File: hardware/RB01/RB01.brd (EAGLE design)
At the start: 50 x 31 mm, 11 parts, among them J1 CON_TERMINAL_BLOCK_03-5MM, J2 CON_TERMINAL_BLOCK_02-5MM, K1 JS-M1-12V-5, Q1 BC337

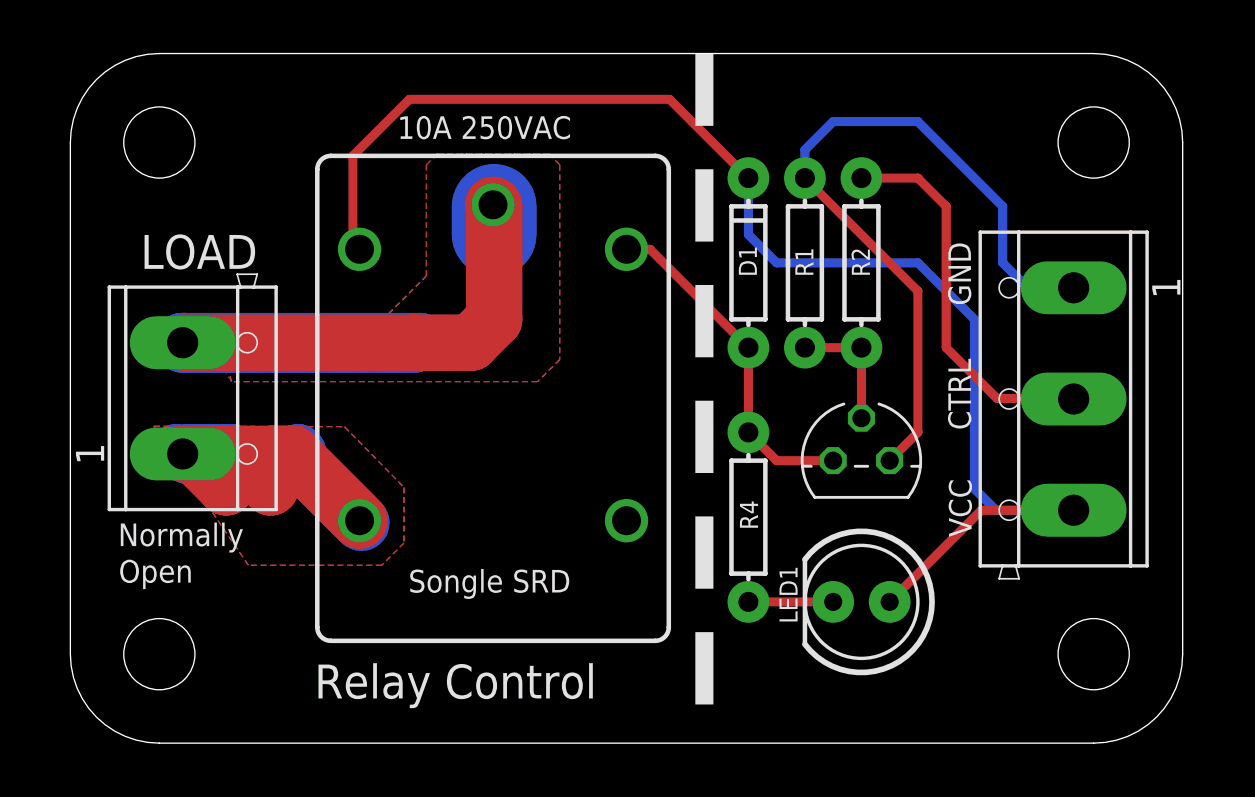
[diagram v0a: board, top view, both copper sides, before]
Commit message: hot traces on bottom only
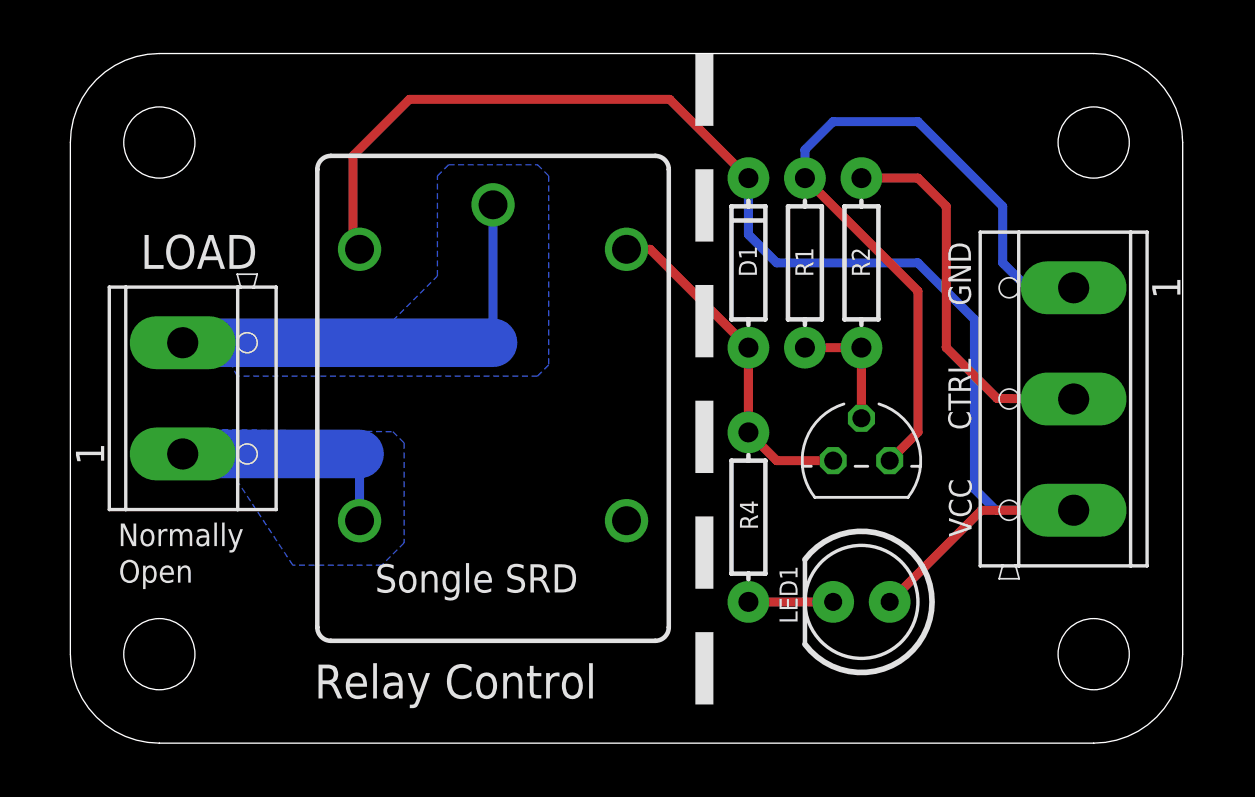
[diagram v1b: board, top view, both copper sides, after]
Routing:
- net LOAD2: track 74.1 -> 20.1 mm
- net LOAD1: track 53.2 -> 10.4 mm
- removed copper zone on layer 1, net LOAD1
- removed copper zone on layer 1, net LOAD2
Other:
- board text removed: "10A 250VAC"
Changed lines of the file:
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@@
 <board>
 <plain>
-<text x="14.692" y="27.162" size="1.016" layer="21" font="vector" ratio="15">10A 250VAC</text>
 <text x="40.483" y="19.661" size="1.016" layer="21" ratio="15" rot="R90">GND</text>
 <text x="40.513" y="9.271" size="1.016" layer="21" ratio="15" rot="R90">VCC</text>
@@
 <text x="2.143" y="8.858" size="1.016" layer="21" ratio="15">Normally</text>
 <text x="40.483" y="14.073" size="1.016" layer="21" ratio="15" rot="R90">CTRL</text>
-<text x="15.192" y="6.772" size="1.016" layer="21" font="vector" ratio="15">Songle SRD</text>
+<text x="13.692" y="6.772" size="1.27" layer="21" font="vector" ratio="15">Songle SRD</text>
 <rectangle x1="16.0163" y1="15.4879" x2="21.5789" y2="15.5133" layer="22" rot="R270"/>
 <rectangle x1="16.0163" y1="15.4879" x2="21.6297" y2="15.5133" layer="22" rot="R270"/>
@@
 <contactref element="K1" pad="C"/>
 <contactref element="J2" pad="2"/>
-<polygon width="0.254" layer="1">
+<polygon width="0.254" layer="16">
 <vertex x="6.746" y="17.97"/>
 <vertex x="8" y="19" curve="-60"/>
 <vertex x="8.1" y="19"/>
-<vertex x="14" y="19"/>
-<vertex x="16" y="21"/>
-<vertex x="16" y="26"/>
-<vertex x="16.5" y="26.5"/>
-<vertex x="21.5" y="26.5"/>
-<vertex x="22" y="26"/>
-<vertex x="22" y="17.25"/>
-<vertex x="21" y="16.25"/>
-<vertex x="7.25" y="16.25"/>
+<vertex x="14.5" y="19"/>
+<vertex x="16.5" y="21"/>
+<vertex x="16.5" y="25.5"/>
+<vertex x="17" y="26"/>
+<vertex x="21" y="26"/>
+<vertex x="21.5" y="25.5"/>
+<vertex x="21.5" y="17"/>
+<vertex x="21" y="16.5"/>
+<vertex x="7.5" y="16.5"/>
 </polygon>
-<polygon width="0.254" layer="16">
-<vertex x="6.246" y="17.97"/>
-<vertex x="8" y="19" curve="-60"/>
-<vertex x="8.1" y="19"/>
-<vertex x="14" y="19"/>
-<vertex x="16" y="21"/>
-<vertex x="16" y="26"/>
-<vertex x="16.5" y="26.5"/>
-<vertex x="21.5" y="26.5"/>
-<vertex x="22" y="26"/>
-<vertex x="22" y="17.25"/>
-<vertex x="21" y="16.25"/>
-<vertex x="7.25" y="16.25"/>
-</polygon>
-<wire x1="5.08" y1="18.034" x2="15.216" y2="18.034" width="2.1844" layer="16"/>
-<wire x1="15.216" y1="18.034" x2="15.5" y2="17.75" width="2.1844" layer="16"/>
-<wire x1="15.5" y1="17.75" x2="5" y2="17.75" width="2.1844" layer="16"/>
-<wire x1="5" y1="17.75" x2="15.25" y2="17.75" width="2.1844" layer="16"/>
-<wire x1="15.25" y1="17.75" x2="15.75" y2="18.25" width="2.1844" layer="16"/>
-<wire x1="15.75" y1="18.25" x2="5" y2="18.25" width="2.1844" layer="16"/>
-<wire x1="5" y1="18.25" x2="15.494" y2="18.034" width="2.1844" layer="16"/>
-<wire x1="5.05" y1="18" x2="15.46" y2="18" width="2.54" layer="1"/>
-<wire x1="15.46" y1="18" x2="18" y2="18" width="2.54" layer="1"/>
-<wire x1="18" y1="18" x2="19.05" y2="19.05" width="2.54" layer="1"/>
-<wire x1="19.05" y1="19.05" x2="19.05" y2="21.59" width="2.54" layer="1"/>
-<wire x1="19.05" y1="21.59" x2="19.05" y2="24.15" width="2.54" layer="1"/>
-<wire x1="19.05" y1="24.15" x2="19" y2="24.2" width="2.54" layer="1"/>
-<wire x1="19.05" y1="24.13" x2="19.05" y2="22.86" width="3.81" layer="16"/>
+<wire x1="5.05" y1="18" x2="19" y2="18" width="2.1844" layer="16"/>
+<wire x1="19" y1="18" x2="19" y2="24.2" width="0.4064" layer="16"/>
 </signal>
 <signal name="LOAD1">
 <contactref element="K1" pad="NO"/>
 <contactref element="J2" pad="1"/>
-<polygon width="0.254" layer="1">
-<vertex x="12.319" y="14.224"/>
-<vertex x="12.327" y="14.216"/>
-<vertex x="15" y="11.5"/>
+<polygon width="0.254" layer="16">
+<vertex x="14.5" y="14"/>
+<vertex x="15" y="13.5"/>
 <vertex x="15" y="9"/>
 <vertex x="14" y="8"/>
-<vertex x="8" y="8"/>
-<vertex x="3.75" y="14.25"/>
+<vertex x="10" y="8"/>
+<vertex x="5.9732375" y="14.101134375"/>
 </polygon>
-<wire x1="5.05" y1="13" x2="7" y2="13" width="2.54" layer="1"/>
-<wire x1="7" y1="13" x2="5.5" y2="13" width="2.54" layer="1"/>
-<wire x1="5.5" y1="13" x2="7" y2="11.5" width="2.54" layer="1"/>
-<wire x1="7" y1="11.5" x2="6" y2="13" width="2.54" layer="1"/>
-<wire x1="6" y1="13" x2="10" y2="13" width="2.54" layer="1"/>
-<wire x1="10" y1="13" x2="9" y2="12" width="2.54" layer="1"/>
-<wire x1="9" y1="12" x2="9" y2="11.5" width="2.54" layer="1"/>
-<wire x1="9" y1="11.5" x2="9" y2="13" width="2.54" layer="1"/>
-<wire x1="9" y1="13" x2="10" y2="13" width="2.54" layer="1"/>
-<wire x1="10" y1="13" x2="13" y2="10" width="2.54" layer="1"/>
-<polygon width="0.254" layer="16">
-<vertex x="12.319" y="14.224"/>
-<vertex x="12.327" y="14.216"/>
-<vertex x="15" y="11.5"/>
-<vertex x="15" y="9"/>
-<vertex x="14" y="8"/>
-<vertex x="8" y="8"/>
-<vertex x="3.75" y="14.25"/>
-</polygon>
-<wire x1="5.08" y1="13.081" x2="4.75" y2="13.25" width="2.1844" layer="16"/>
-<wire x1="4.75" y1="13.25" x2="5.25" y2="12.75" width="2.1844" layer="16"/>
-<wire x1="5.25" y1="12.75" x2="6.5" y2="12.75" width="2.1844" layer="16"/>
-<wire x1="6.5" y1="12.75" x2="6.5" y2="12.5" width="2.1844" layer="16"/>
-<wire x1="6.5" y1="12.5" x2="7.5" y2="12.75" width="2.1844" layer="16"/>
-<wire x1="7.5" y1="12.75" x2="7.25" y2="13" width="2.1844" layer="16"/>
-<wire x1="7.25" y1="13" x2="5" y2="13" width="2.1844" layer="16"/>
-<wire x1="5" y1="13" x2="5.25" y2="13.25" width="2.1844" layer="16"/>
-<wire x1="5.25" y1="13.25" x2="7.5" y2="13" width="2.1844" layer="16"/>
-<wire x1="7.5" y1="13" x2="7.25" y2="13.25" width="2.1844" layer="16"/>
-<wire x1="7.25" y1="13.25" x2="5.5" y2="13.25" width="2.1844" layer="16"/>
-<wire x1="5.5" y1="13.25" x2="5.5" y2="13" width="2.1844" layer="16"/>
-<wire x1="5.5" y1="13" x2="6.5" y2="13" width="2.1844" layer="16"/>
-<wire x1="6.5" y1="13" x2="6.5" y2="12.75" width="2.1844" layer="16"/>
-<wire x1="6.5" y1="12.5" x2="6" y2="12.5" width="2.1844" layer="16"/>
-<wire x1="6" y1="12.5" x2="10.25" y2="13.25" width="2.1844" layer="16"/>
-<wire x1="10.25" y1="13.25" x2="10.406" y2="13.094" width="2.1844" layer="16"/>
-<wire x1="10.406" y1="13.094" x2="7" y2="11.5" width="2.1844" layer="16"/>
-<wire x1="7" y1="11.5" x2="5.406" y2="13.094" width="2.1844" layer="16"/>
-<wire x1="5.406" y1="13.094" x2="5" y2="13.094" width="2.1844" layer="16"/>
-<wire x1="5" y1="13.094" x2="5" y2="13" width="2.1844" layer="16"/>
-<wire x1="5" y1="13" x2="10.406" y2="12.581" width="2.1844" layer="16"/>
-<wire x1="10.406" y1="12.581" x2="13.081" y2="9.906" width="2.54" layer="16"/>
+<wire x1="5.05" y1="13" x2="13" y2="13" width="2.1844" layer="16"/>
+<wire x1="13" y1="13" x2="13" y2="10.5" width="0.4064" layer="16"/>
 </signal>
 <signal name="VCC">

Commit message: faster higher-power diode closer to coil
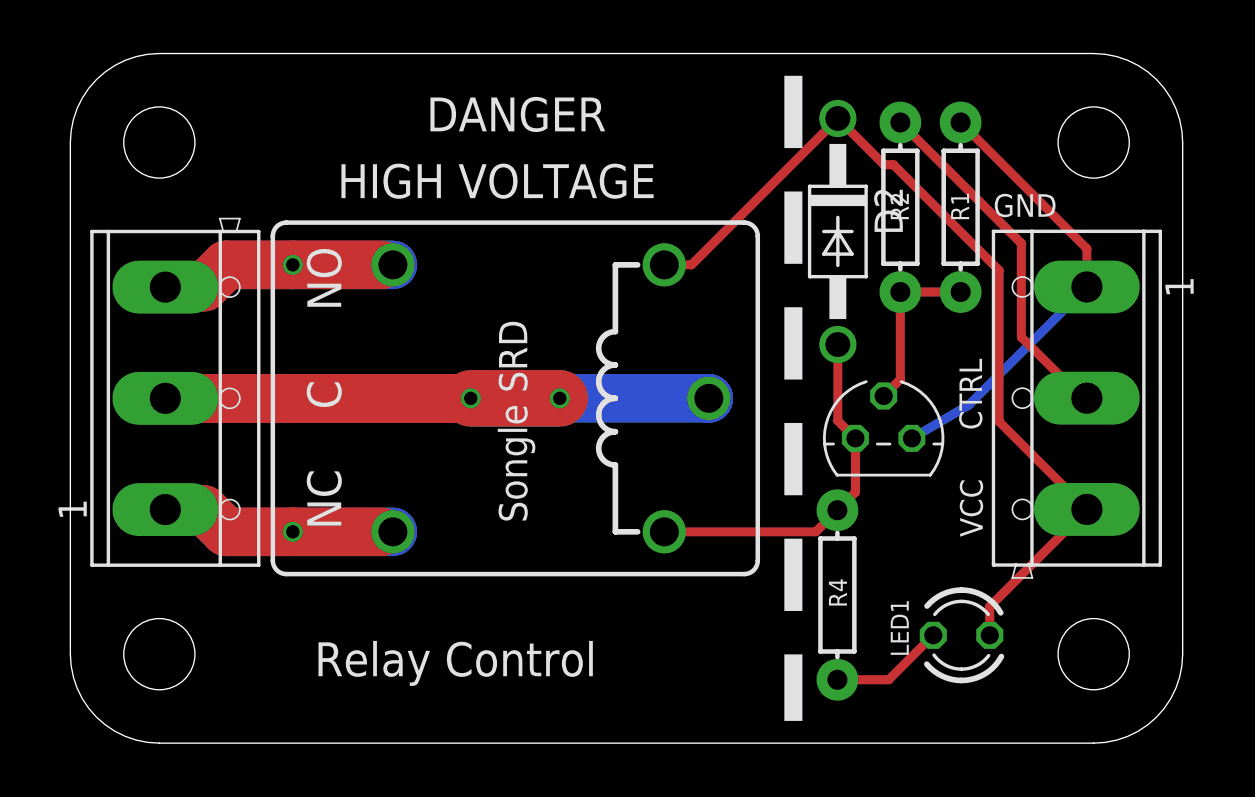
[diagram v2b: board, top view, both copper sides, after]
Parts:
- removed D1: 1N4148, SparkFun:DIODE-1N4148
- added D2: 1N4936, diode:DO41-10
- J2: value CON_TERMINAL_BLOCK_02-5MM -> CON_TERMINAL_BLOCK_03-5MM; device dp_devices:TERMINAL_BLOCK_2P_5 -> dp_devices:TERMINAL_BLOCK_3P_5
- LED1: device SparkFun:LED5MM -> dp_devices:LED-3MM
- moved R1 7.43 mm to (40.0, 24.1)
- moved U$2 5.50 mm to (13.0, 5.58)
- moved R4 5.32 mm to (34.5, 6.66)
- moved LED1 4.74 mm to (40.1, 4.85)
- moved R2 3.05 mm to (37.3, 24.1)
- moved Q1 1.41 mm to (36.6, 13.7)
- moved K1 1.00 mm to (20.0, 15.5), turned to 0 degrees
- moved J2 0.78 mm to (4.72, 15.5)
- moved J1 0.60 mm to (45.2, 15.5)
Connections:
- net LOAD2 renamed C
- removed net LOAD1: J2.1, K1.NO
- new net NC: J2.1, K1.NC
- new net NO: J2.3, K1.NO
- net COIL: now also D2.A; no longer D1.A
- net VCC: now also D2.C; no longer D1.C
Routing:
- net C: track 20.1 -> 65.7 mm, vias 0 -> 2
- net VCC: track 61.4 -> 40.4 mm
- net NC: track 0.00 -> 20.1 mm, vias 0 -> 1
- net NO: track 0.00 -> 20.1 mm, vias 0 -> 1
- net GND: track 33.9 -> 20.2 mm
- net LOAD1: track 10.4 -> 0.00 mm
- net N$6: track 5.71 -> 7.70 mm
- net RELAY: track 17.4 -> 16.0 mm
- net N$9: track 3.81 -> 5.14 mm
- net COIL: track 15.5 -> 16.3 mm
- removed copper zone on layer 16, net C
- removed copper zone on layer 16, net LOAD1
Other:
- board text added: "C"
- board text added: "HIGH VOLTAGE"
- board text added: "Magic Smoke"
- board text added: "NC"
- board text added: "NO"
- board text added: "RB01"
- board text removed: "LOAD"
- board text removed: "Magic Smoke RB01"
- board text removed: "Normally"
- board text removed: "Open"
